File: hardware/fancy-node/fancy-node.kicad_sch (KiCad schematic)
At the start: 64 parts, among them J1 USB_B_Micro, J2 Conn_01x06, J3 Conn_01x03, J4 Conn_01x03, J5 Conn_01x04, J6 Conn_01x02, J7 2337019-1, SW1 SW_Push, SW2 SW_Push, SW3 SW_Push, SW4 SW_SPDT, U1 CH340X, U2 STM32G030C8T6, U3 WS2812b, U4 HT75xx-1-SOT89, U5 RFM69CW-915MHZ, U6 TP4056

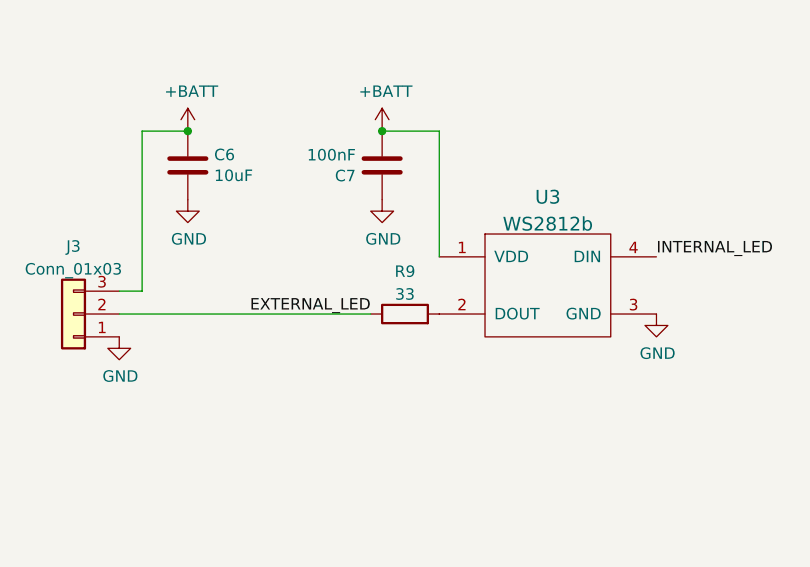
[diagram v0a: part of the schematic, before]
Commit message: DFM tweaks for fancy-node v1.2
Change-Id: I792b47978d6c444ab90a5a071e11440810b06c61
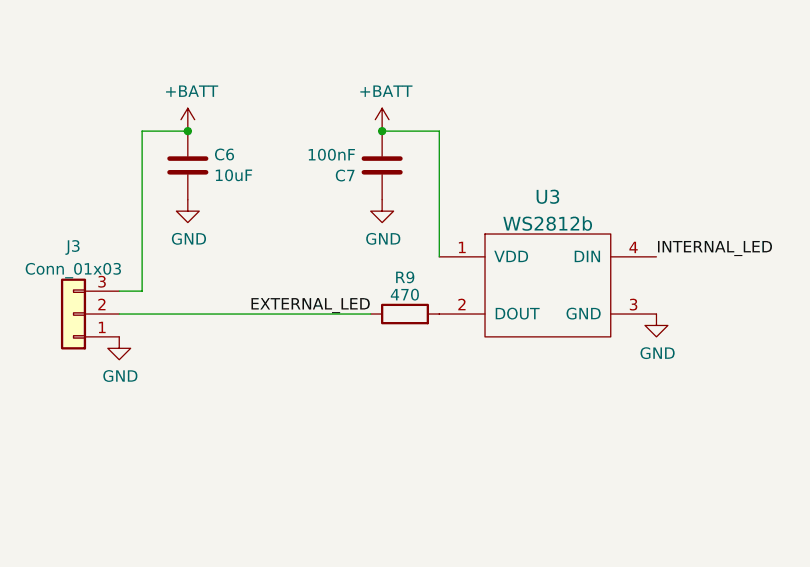
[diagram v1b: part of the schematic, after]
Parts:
- R9: value 33 -> 470; footprint Resistor_SMD:R_0402_1005Metric -> Resistor_SMD:R_0603_1608Metric; LCSC C25105 -> C23179
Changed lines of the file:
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@@
   (symbol (lib_id "Device:R") (at 224.79 210.82 90) (unit 1)
     (in_bom yes) (on_board yes) (dnp no) (fields_autoplaced)
-    (property "Reference" "R9" (at 224.79 206.1042 90)
+    (property "Reference" "R9" (at 224.79 206.7941 90)
       (effects (font (size 1.27 1.27)))
     )
-    (property "Value" "33" (at 224.79 208.6411 90)
+    (property "Value" "470" (at 224.79 208.7151 90)
       (effects (font (size 1.27 1.27)))
     )
-    (property "Footprint" "Resistor_SMD:R_0402_1005Metric" (at 224.79 212.598 90)
+    (property "Footprint" "Resistor_SMD:R_0603_1608Metric" (at 224.79 212.598 90)
       (effects (font (size 1.27 1.27)) hide)
     )
@@
       (effects (font (size 1.27 1.27)) hide)
     )
-    (property "LCSC" "C25105" (at 224.79 210.82 90)
+    (property "LCSC" "C23179" (at 224.79 210.82 90)
       (effects (font (size 1.27 1.27)) hide)
     )

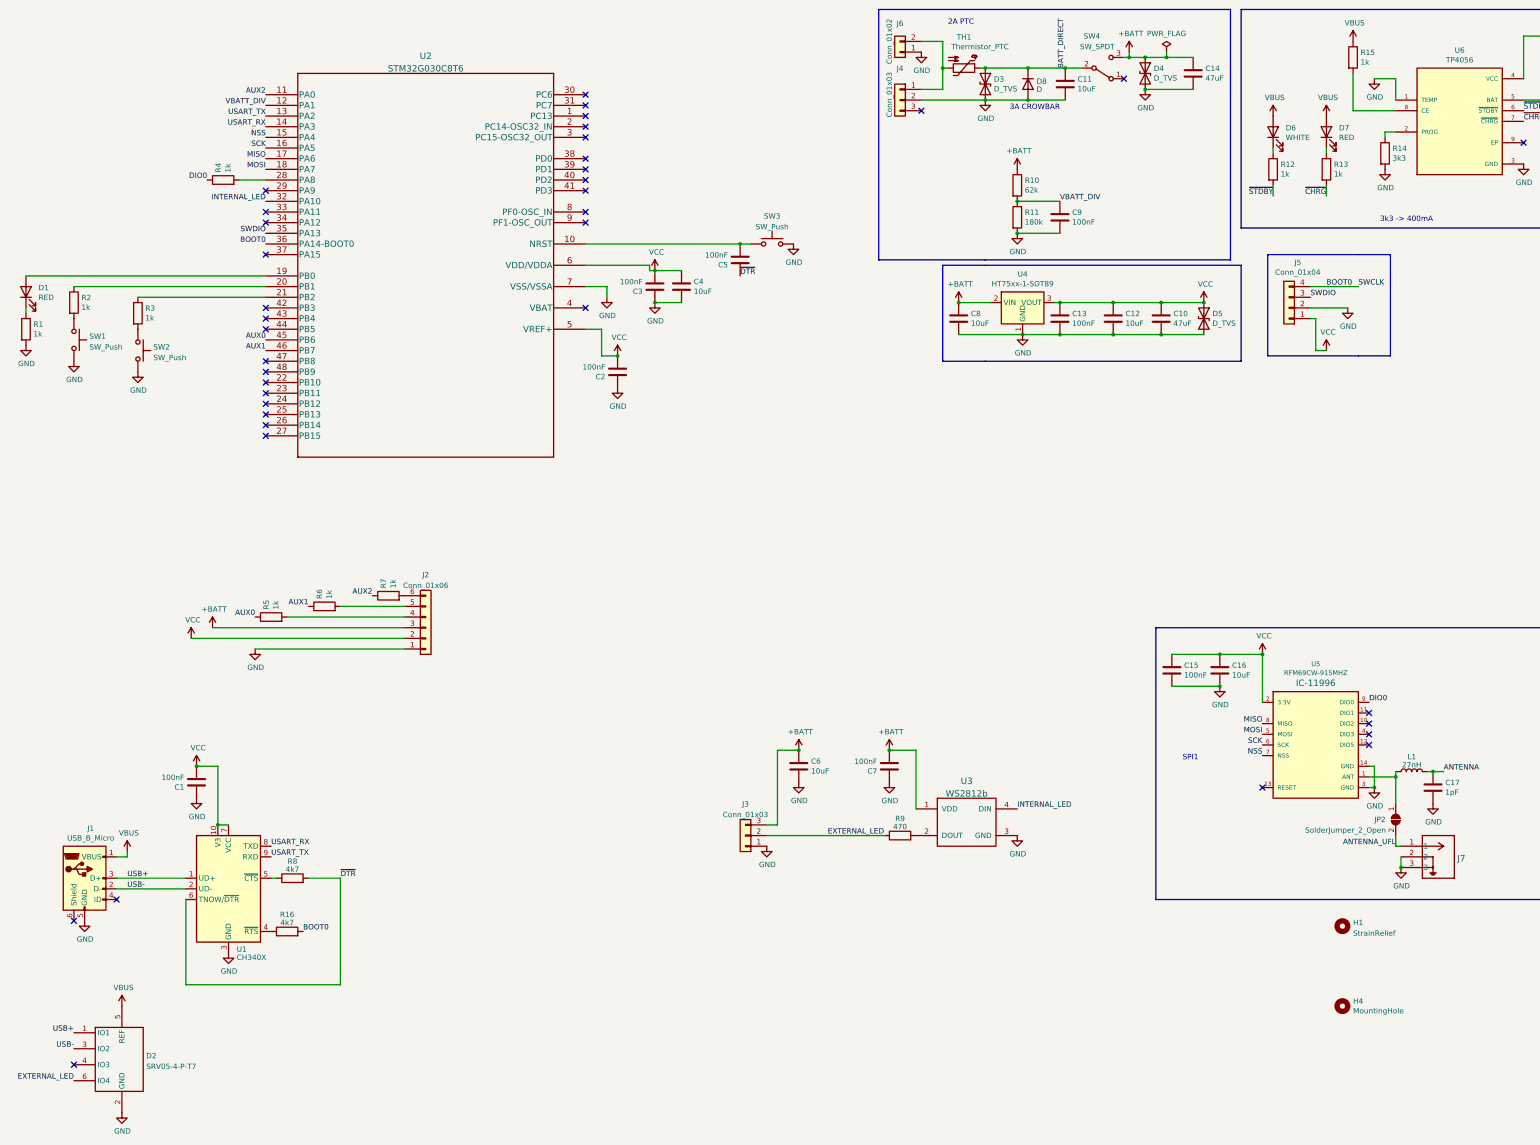
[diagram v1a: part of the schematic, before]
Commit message: fancy-node v1.3:
- Migrate to MCU with 128kB of flash, from 64kB
- Fix power switch labels
- Fix bootloader: use "One-click USB download of MCU" configuration from CH340 datasheet
- Update pi filter for antenna tuning, based on NanoVNA measurement

Change-Id: I47198b318729be310c11fabc2dad25f322eb5a4f
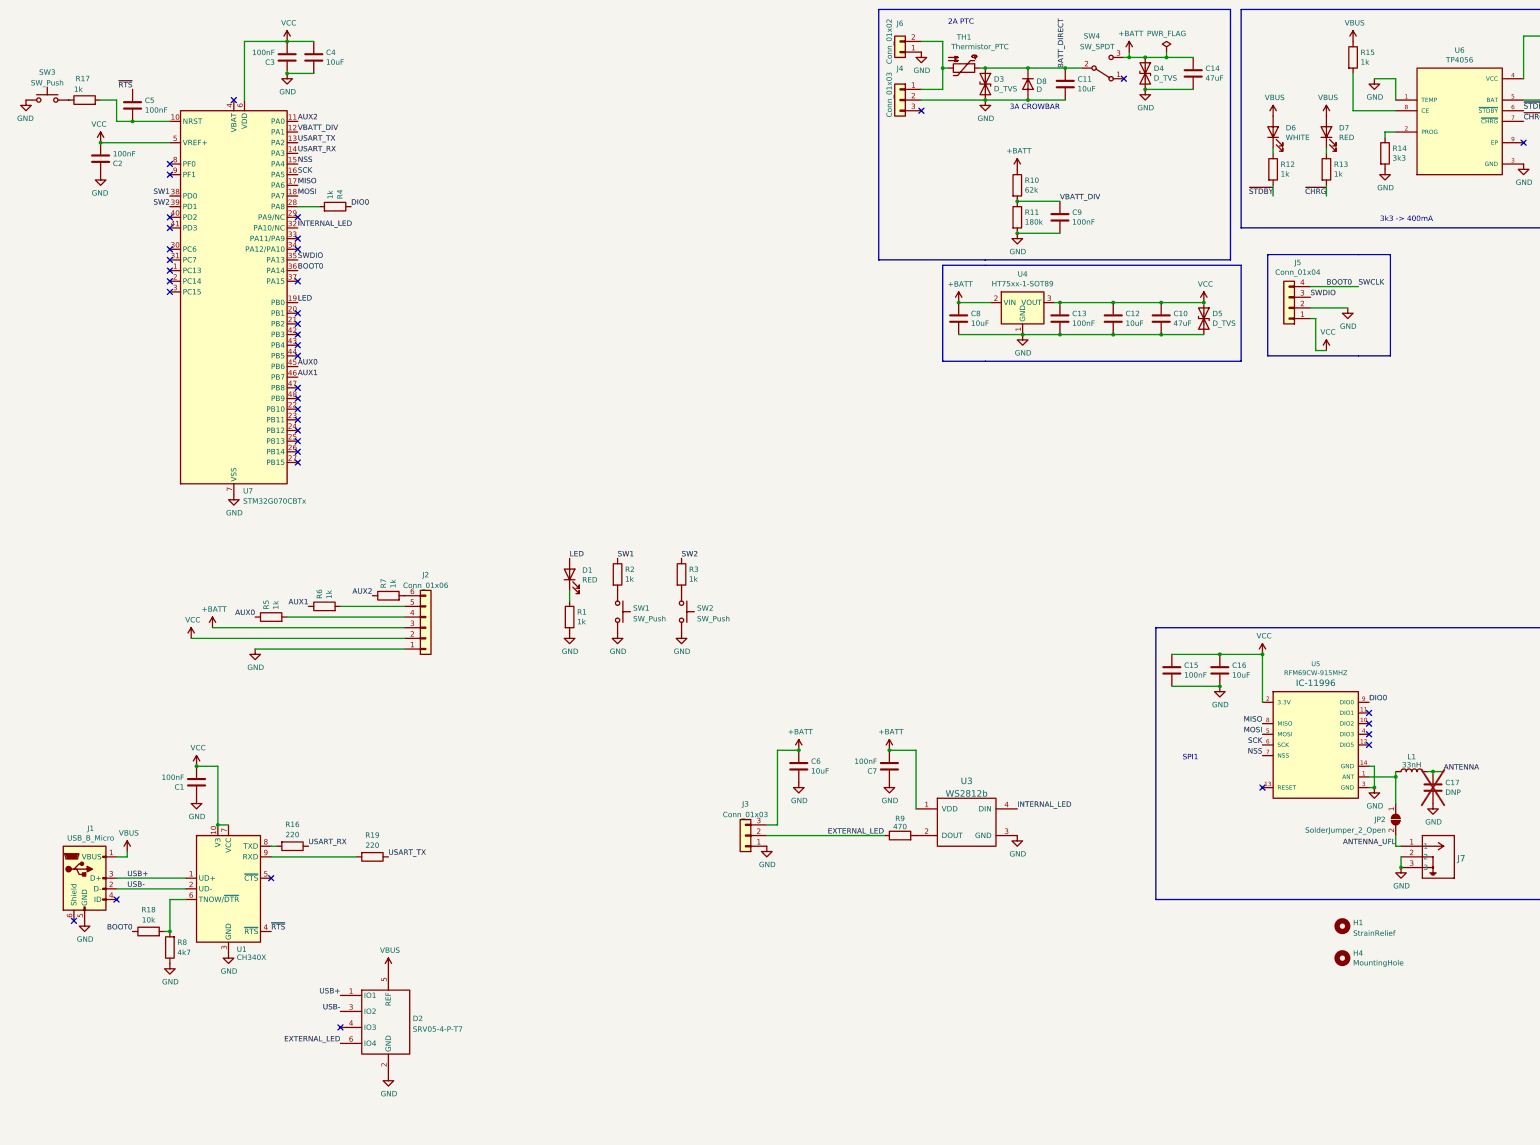
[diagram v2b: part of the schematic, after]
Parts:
- removed U2: STM32G030C8T6, Package_QFP:LQFP-48_7x7mm_P0.5mm, symbol Homebrew:STM32G030C8T6
- added R17: 1k, Resistor_SMD:R_0402_1005Metric, symbol Device:R
- added R18: 10k, Resistor_SMD:R_0402_1005Metric, symbol Device:R
- added R19: 220, Resistor_SMD:R_0402_1005Metric, symbol Device:R
- added U7: STM32G070CBTx, Package_QFP:LQFP-48_7x7mm_P0.5mm, symbol MCU_ST_STM32G0:STM32G070CBTx
- C17: value 1pF -> DNP; now not fitted
- L1: value 27nH -> 33nH; LCSC C2041663 -> C113114
- R16: value 4k7 -> 220; LCSC C25900 -> C25091
- U5: footprint Homebrew:RFM69CW-minimalpads -> RFM69CW-XXXS2
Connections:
- net AUX0: now also U7.45 (PB6)
- net AUX1: now also U7.46 (PB7)
- net AUX2: now also U7.11 (PA0)
- net BOOT0: now also R18.1, U7.36 (PA14); no longer R16.2
- net GND: now also R8.1, U7.7 (VSS)
- net INTERNAL_LED: now also U7.32 (PA10/NC)
- net MISO: now also U7.17 (PA6)
- net MOSI: now also U7.18 (PA7)
- net NSS: now also U7.15 (PA4)
- net SCK: now also U7.16 (PA5)
- net SWDIO: now also U7.35 (PA13)
- net USART_RX: now also R16.1, U7.14 (PA3); no longer U1.8 (TXD)
- net USART_TX: now also R19.1, U7.13 (PA2); no longer U1.9 (RXD)
- net VBATT_DIV: now also U7.12 (PA1)
- net VCC: now also U7.5 (VREF+), U7.6 (VDD)
- net at C5.2: now also R17.2, U7.10 (NRST); no longer SW3.1
- net LED: now reaches D1.2 (A)
- net LED: now also U7.19 (PB0)
- net SW1: now reaches R2.1
- net SW1: now also U7.38 (PD0)
- net SW2: now reaches R3.1
- net SW2: now also U7.39 (PD1)
- net at R4.2: now also U7.28 (PA8)
- net ~{RTS}: now reaches U1.4 (~{RTS})
- net ~{RTS}: now also C5.1; no longer R16.1
- net at U1.5 (~{CTS}): no longer R8.1
- net ~{DTR}: no longer names the net of R8.2, U1.6 (TNOW/~{DTR})
- net ~{DTR}: now also R18.2; no longer C5.1
- new net: R16.2, U1.8 (TXD)
- new net: R19.2, U1.9 (RXD)
- new net: R17.1, SW3.1
- no-connect marks 38 -> 39
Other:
- moved on the sheet: C2, C3, C4, C5, D1, D2, H4, R1, R2, R3, R4, R8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
